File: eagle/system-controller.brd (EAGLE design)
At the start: 99 x 100 mm, 227 parts, among them J1 1, Q1 MOSFET-P-N-PAIR, Q10 MOSFET-P-N-PAIR, Q11 DNP/NTR4101P, Q2 MOSFET-P-N-PAIR, Q3 DON3035L, Q4 MOSFET-P-N-PAIR, Q5 MOSFET-P-N-PAIR, Q6 MOSFET-P-N-PAIR, Q7 MOSFET-P-N-PAIR, Q8 MOSFET-P-N-PAIR, Q9 DNP/NTR4101P, U1 TPS25944LRVCRWQFN-20-3X4, U10 TPS25944LRVCRWQFN-20-3X4, U11 ACPL-M61L, U12 ACPL-M61L, U13 TPS25944LRVCRWQFN-20-3X4, U14 ACPL-M61L, U15 ACPL-M61L, U2 LP5907MFX-3.0, U3 TPS25944LRVCRWQFN-20-3X4, U4 TPS25944LRVCRWQFN-20-3X4, U5 TPS25944LRVCRWQFN-20-3X4, U6 TPS25944LRVCRWQFN-20-3X4, U7 ATMEGA128L-8A(U/N), U8 TS4100, U9 TPS25944LRVCRWQFN-20-3X4, X1 8 MHz CRYSTAL-ABRACON-ABM3-SMD

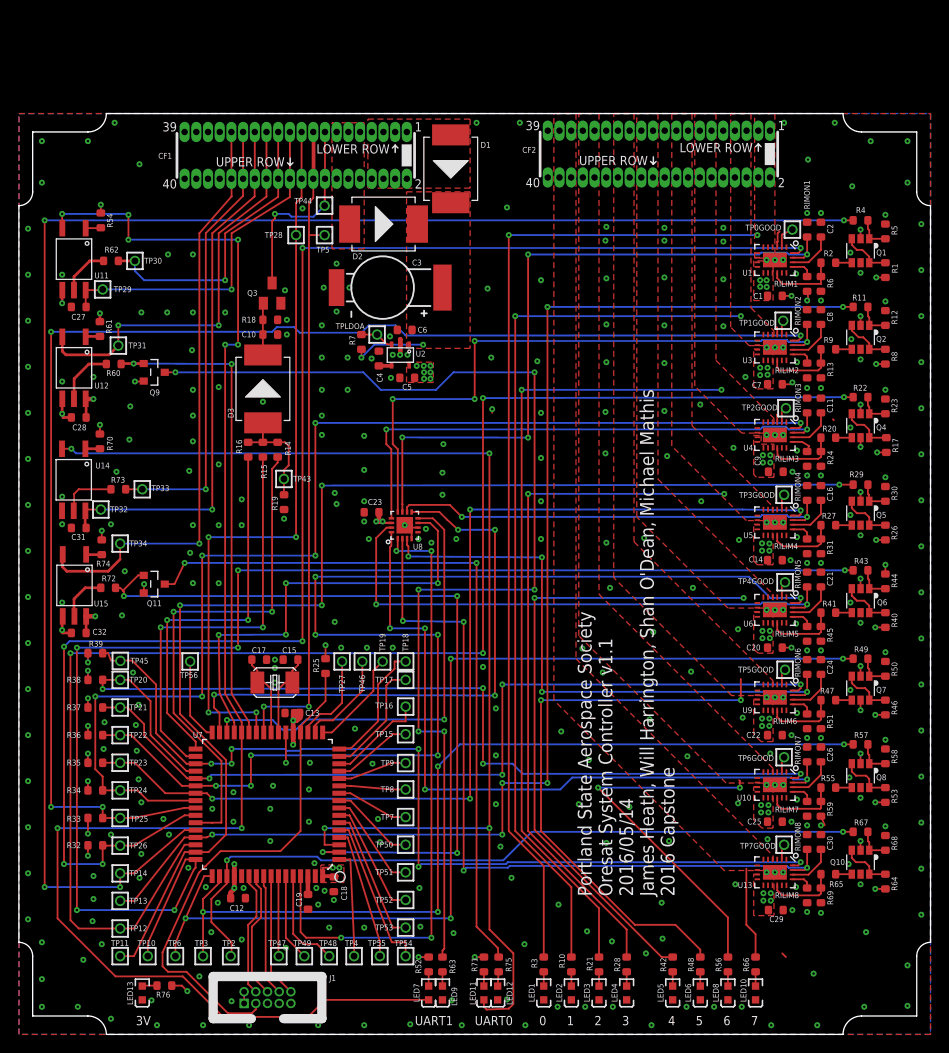
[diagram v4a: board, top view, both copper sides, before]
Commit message: added missing datasheets
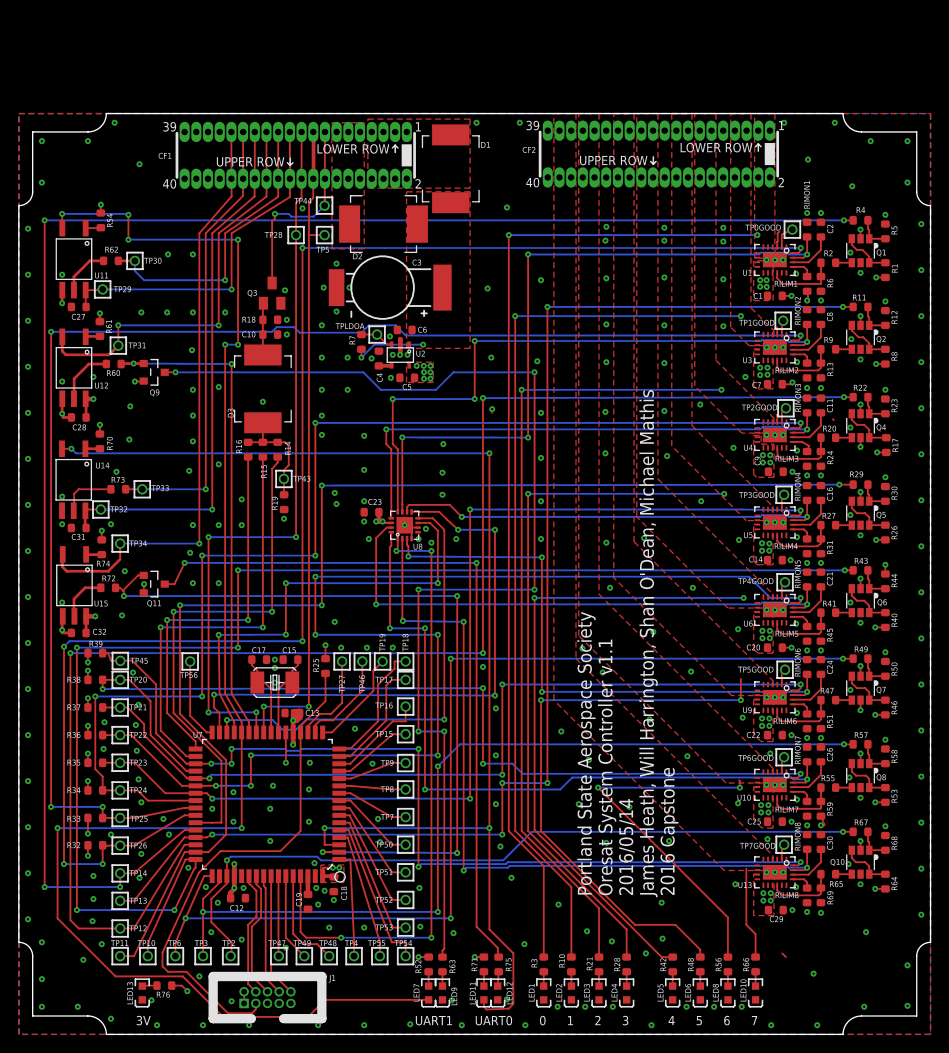
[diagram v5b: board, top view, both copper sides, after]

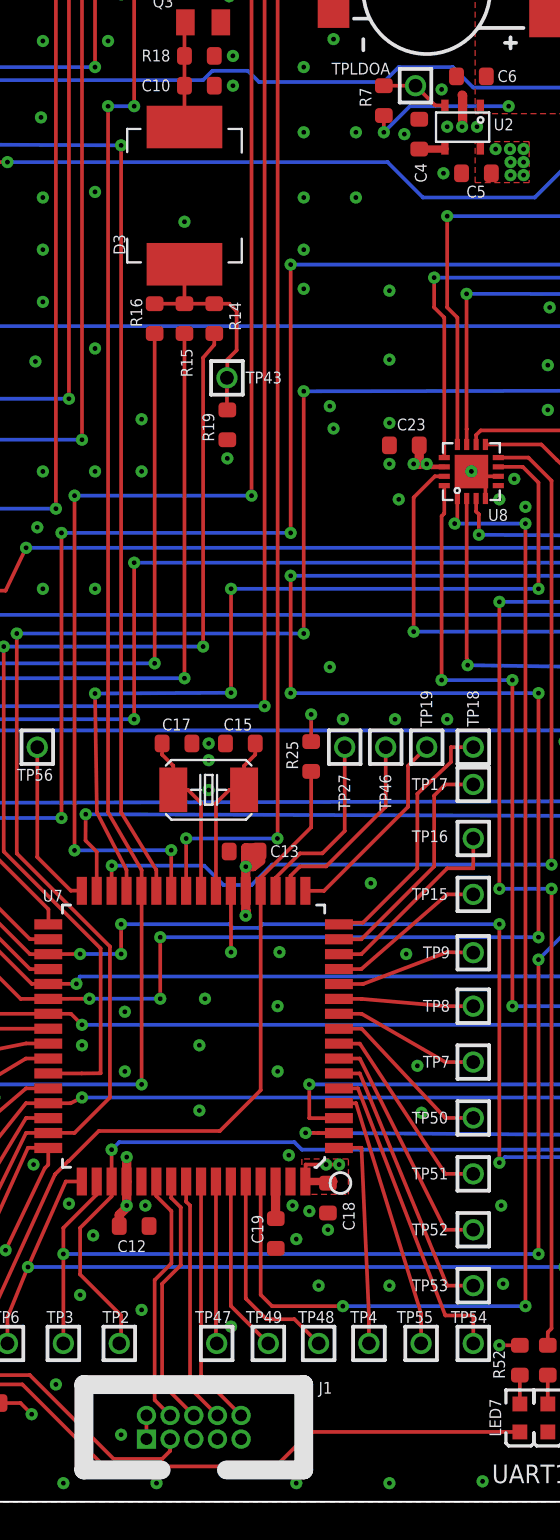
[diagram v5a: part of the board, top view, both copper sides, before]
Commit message: Fixed some of the remaining issues such as JTAG layout and schematic, 0 ohm resistors, etc. Check the issue section on the git for more info
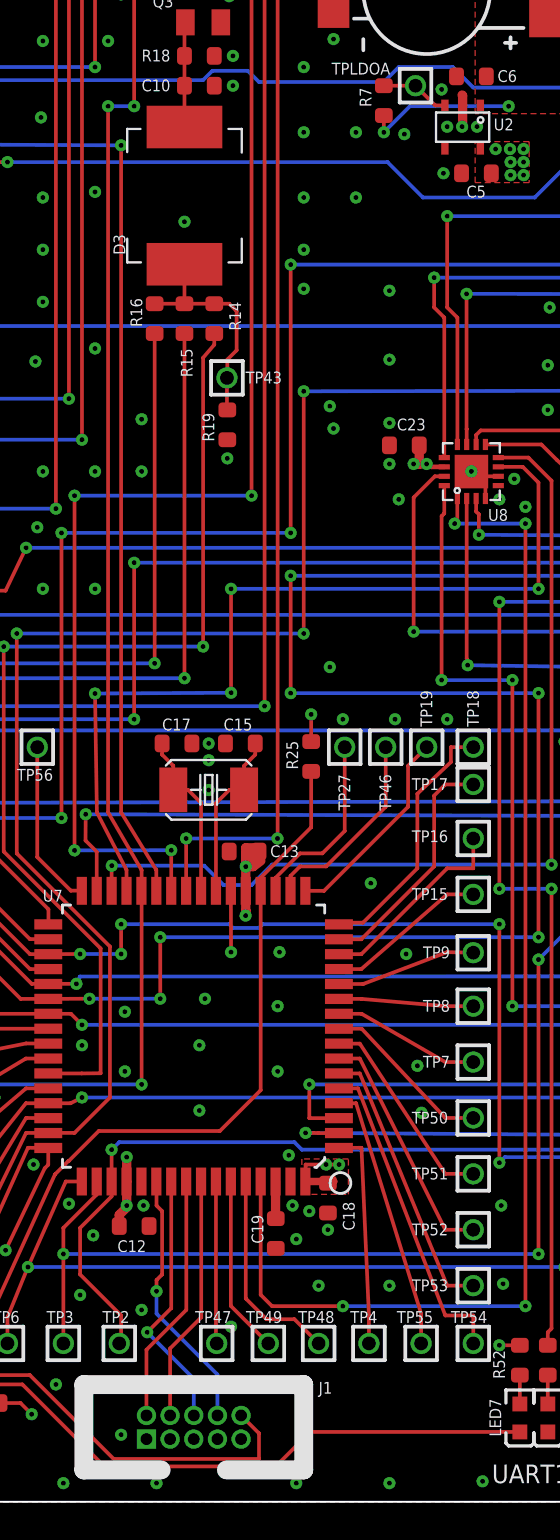
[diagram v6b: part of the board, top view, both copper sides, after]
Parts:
- removed C4: 10nF, rcl_custom:.0603-B-NOSILK
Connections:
- removed net N$23: C4.1, U2.4
- net 3V: no longer J1.2
- net GND: now also J1.3, J1.5; no longer C4.2, J1.7
- net N$11: now also J1.4; no longer J1.10
- net N$13: now also U7.54; no longer U7.56
- net N$14: now also J1.2, U7.56; no longer J1.4, U7.54
- net N$15: now also J1.10; no longer J1.3
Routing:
- net N$15: track 55.3 -> 61.9 mm
- net N$23: track 1.38 -> 0.00 mm
- net 3V: track 46.7 -> 45.5 mm
- net N$13: track 13.3 -> 14.2 mm, vias 0 -> 1
- net N$12: track 13.9 -> 14.1 mm, vias 0 -> 1
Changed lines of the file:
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@@
 <?xml version="1.0" encoding="utf-8"?>
 <!DOCTYPE eagle SYSTEM "eagle.dtd">
-<eagle version="7.5.0">
+<eagle version="7.6.0">
 <drawing>
 <settings>
@@
 <attribute name="NAME" x="42.17" y="71.3" size="0.3" layer="33" ratio="15" rot="R180" align="center"/>
 </element>
-<element name="C4" library="rcl_custom" package=".0603-B-NOSILK" value="10nF" x="39.1" y="73.4" smashed="yes" rot="R90">
-<attribute name="DIST" value="digikey" x="39.1" y="73.4" size="1.778" layer="27" rot="R90" display="off"/>
-<attribute name="DPN" value="399-1092-1-ND" x="39.1" y="73.4" size="1.778" layer="27" rot="R90" display="off"/>
-<attribute name="MFN" value="Kemet" x="39.1" y="73.4" size="1.778" layer="27" rot="R90" display="off"/>
-<attribute name="MPN" value="C0603C103J5RACTU" x="39.1" y="73.4" size="1.778" layer="27" rot="R90" display="off"/>
-<attribute name="NAME" x="39.5" y="70.8" size="0.635" layer="25" font="vector" ratio="20" rot="R90"/>
-<attribute name="VALUE" x="39.8" y="75.2" size="0.635" layer="27" font="vector" ratio="15" rot="R90"/>
-<attribute name="NAME" x="39.1" y="73.4" size="0.3" layer="33" ratio="15" rot="R90" align="center"/>
-</element>
 <element name="C15" library="rcl_custom" package=".0603-B-NOSILK" value="9pF" x="29.5" y="40.7" smashed="yes">
 <attribute name="DIST" value="digikey" x="29.5" y="40.7" size="1.778" layer="27" display="off"/>
@@
 <via x="43.9" y="74.9" extent="1-16" drill="0.254"/>
 </signal>
-<signal name="N$11">
-<contactref element="U7" pad="57"/>
-<contactref element="J1" pad="10"/>
-<wire x1="27.39" y1="17.19" x2="27.39" y2="6.785" width="0.2" layer="1"/>
-<wire x1="27.39" y1="6.785" x2="29.54" y2="4.635" width="0.2" layer="1"/>
-</signal>
-<signal name="N$12">
-<contactref element="U7" pad="55"/>
-<contactref element="J1" pad="6"/>
-<wire x1="25.3" y1="6.335" x2="27" y2="4.635" width="0.2" layer="1"/>
-<wire x1="25.79" y1="17.19" x2="25.79" y2="16.31" width="0.2" layer="1"/>
-<wire x1="25.79" y1="16.31" x2="26.3" y2="15.8" width="0.2" layer="1"/>
-<wire x1="26.3" y1="15.8" x2="26.3" y2="12.7" width="0.2" layer="1"/>
-<wire x1="26.3" y1="12.7" x2="25.3" y2="11.7" width="0.2" layer="1"/>
-<wire x1="25.3" y1="11.7" x2="25.3" y2="6.335" width="0.2" layer="1"/>
-</signal>
-<signal name="N$13">
-<contactref element="U7" pad="56"/>
-<contactref element="J1" pad="8"/>
-<wire x1="26.59" y1="17.19" x2="26.59" y2="16.11" width="0.2" layer="1"/>
-<wire x1="26.59" y1="16.11" x2="26.8" y2="15.9" width="0.2" layer="1"/>
-<wire x1="26.8" y1="15.9" x2="26.8" y2="6.105" width="0.2" layer="1"/>
-<wire x1="26.8" y1="6.105" x2="28.27" y2="4.635" width="0.2" layer="1"/>
-</signal>
-<signal name="N$14">
-<contactref element="U7" pad="54"/>
-<contactref element="J1" pad="4"/>
-<wire x1="24.9" y1="5.465" x2="25.73" y2="4.635" width="0.2" layer="1"/>
-<wire x1="24.99" y1="17.19" x2="24.99" y2="16.41" width="0.2" layer="1"/>
-<wire x1="24.99" y1="16.41" x2="25.8" y2="15.6" width="0.2" layer="1"/>
-<wire x1="25.8" y1="15.6" x2="25.8" y2="12.8" width="0.2" layer="1"/>
-<wire x1="25.8" y1="12.8" x2="24.9" y2="11.9" width="0.2" layer="1"/>
-<wire x1="24.9" y1="11.9" x2="24.9" y2="5.465" width="0.2" layer="1"/>
-</signal>
 <signal name="N$15">
 <contactref element="U7" pad="20"/>
 <contactref element="R25" pad="2"/>
-<contactref element="J1" pad="3"/>
 <wire x1="19.55" y1="17.57" x2="16.1" y2="10" width="0.2" layer="1"/>
 <wire x1="16.1" y1="10" x2="15.6" y2="8.9" width="0.2" layer="1"/>
@@
 <wire x1="16.2" y1="6.8" x2="18.2" y2="6.8" width="0.2" layer="1"/>
 <wire x1="18.2" y1="6.8" x2="22.7" y2="2.3" width="0.2" layer="1"/>
-<wire x1="22.7" y1="2.3" x2="25.3" y2="2.3" width="0.2" layer="1"/>
-<wire x1="25.3" y1="2.3" x2="25.73" y2="2.73" width="0.2" layer="1"/>
-<wire x1="25.7" y1="3.335" x2="25.73" y2="3.365" width="0.2" layer="1"/>
-<wire x1="25.73" y1="3.365" x2="25.73" y2="2.73" width="0.2" layer="1"/>
+<contactref element="J1" pad="10"/>
+<wire x1="22.7" y1="2.3" x2="30.5" y2="2.3" width="0.2" layer="1"/>
+<wire x1="30.5" y1="2.3" x2="30.5" y2="3.675" width="0.2" layer="1"/>
+<wire x1="30.5" y1="3.675" x2="29.54" y2="4.635" width="0.2" layer="1"/>
 </signal>
 <signal name="PCB3_EN">
@@
 <wire x1="6.1" y1="68.91" x2="5.985" y2="69.025" width="0.2" layer="1"/>
 </signal>
-<signal name="N$23">
-<contactref element="C4" pad="1"/>
-<contactref element="U2" pad="4"/>
-<wire x1="39.1" y1="72.6" x2="40.466" y2="72.6" width="0.4" layer="1"/>
-<wire x1="40.466" y1="72.6" x2="40.478" y2="72.612" width="0.4" layer="1"/>
-</signal>
 <signal name="N$1">
 <contactref element="X1" pad="P$2"/>
@@
 <contactref element="R36" pad="1"/>
 <contactref element="R32" pad="1"/>
-<contactref element="J1" pad="2"/>
 <contactref element="U7" pad="64"/>
 <contactref element="U7" pad="21"/>
 <contactref element="U7" pad="52"/>
-<wire x1="24.46" y1="3.365" x2="24.46" y2="4.635" width="0.2" layer="1"/>
 <polygon width="0.2" layer="15" isolate="0.2" thermals="no">
 <vertex x="6" y="90.5"/>
@@
 <signal name="GND">
 <contactref element="C5" pad="2"/>
-<contactref element="C4" pad="2"/>
 <contactref element="C6" pad="1"/>
 <contactref element="C3" pad="-"/>
@@
 <contactref element="C17" pad="1"/>
 <contactref element="J1" pad="9"/>
-<contactref element="J1" pad="7"/>
 <contactref element="C27" pad="1"/>
 <contactref element="C31" pad="1"/>
@@
 <via x="34.2" y="14.6" extent="1-16" drill="0.254"/>
 <via x="33.2" y="15.6" extent="1-16" drill="0.254"/>
-<via x="24.4" y="15.9" extent="1-16" drill="0.254"/>
+<via x="24.3" y="15.9" extent="1-16" drill="0.254"/>
 <via x="27.8" y="38.2" extent="1-16" drill="0.254"/>
 <via x="27.8" y="40.7" extent="1-16" drill="0.254"/>
@@
 <via x="26.5" y="68.7" extent="1-16" drill="0.254"/>
 <contactref element="LED13" pad="K"/>
+<contactref element="J1" pad="5"/>
+<contactref element="J1" pad="3"/>
 </signal>
 <signal name="N$207">
@@
 <wire x1="13.45" y1="5.3" x2="13.4" y2="5.25" width="0.2" layer="1"/>
 </signal>
+<signal name="N$11">
+<contactref element="J1" pad="4"/>
+<contactref element="U7" pad="57"/>
+<wire x1="25.73" y1="4.635" x2="25.73" y2="8.23" width="0.2" layer="1"/>
+<wire x1="25.73" y1="8.23" x2="27.4" y2="9.9" width="0.2" layer="1"/>
+<wire x1="27.4" y1="9.9" x2="27.4" y2="17.18" width="0.2" layer="1"/>
+<wire x1="27.4" y1="17.18" x2="27.39" y2="17.19" width="0.2" layer="1"/>
+</signal>
+<signal name="N$12">
+<contactref element="J1" pad="6"/>
+<contactref element="U7" pad="55"/>
+<wire x1="27" y1="4.635" x2="27" y2="6.6" width="0.2" layer="16"/>
+<wire x1="27" y1="6.6" x2="24.5" y2="9.1" width="0.2" layer="16"/>
+<via x="24.5" y="9.1" extent="1-16" drill="0.254"/>
+<wire x1="24.5" y1="9.1" x2="25.79" y2="10.39" width="0.2" layer="1"/>
+<wire x1="25.79" y1="10.39" x2="25.79" y2="17.19" width="0.2" layer="1"/>
+</signal>
+<signal name="N$13">
+<contactref element="J1" pad="8"/>
+<contactref element="U7" pad="54"/>
+<wire x1="28.27" y1="4.635" x2="28.27" y2="6.83" width="0.2" layer="16"/>
+<wire x1="28.27" y1="6.83" x2="25" y2="10.1" width="0.2" layer="16"/>
+<wire x1="25" y1="10.1" x2="25" y2="11.3" width="0.2" layer="16"/>
+<via x="25" y="11.3" extent="1-16" drill="0.254"/>
+<wire x1="25" y1="11.3" x2="25" y2="11.9" width="0.2" layer="1"/>
+<wire x1="25" y1="11.9" x2="25.3" y2="12.2" width="0.2" layer="1"/>
+<wire x1="25.3" y1="12.2" x2="25.3" y2="15.6" width="0.2" layer="1"/>
+<wire x1="25.3" y1="15.6" x2="25" y2="15.9" width="0.2" layer="1"/>
+<wire x1="25" y1="15.9" x2="25" y2="17.18" width="0.2" layer="1"/>
+<wire x1="25" y1="17.18" x2="24.99" y2="17.19" width="0.2" layer="1"/>
+</signal>
+<signal name="N$14">
+<contactref element="J1" pad="2"/>
+<contactref element="U7" pad="56"/>
+<wire x1="24.46" y1="4.635" x2="24.46" y2="8.16" width="0.2" layer="1"/>
+<wire x1="24.46" y1="8.16" x2="26.6" y2="10.3" width="0.2" layer="1"/>
+<wire x1="26.6" y1="10.3" x2="26.6" y2="17.18" width="0.2" layer="1"/>
+<wire x1="26.6" y1="17.18" x2="26.59" y2="17.19" width="0.2" layer="1"/>
+</signal>
 </signals>

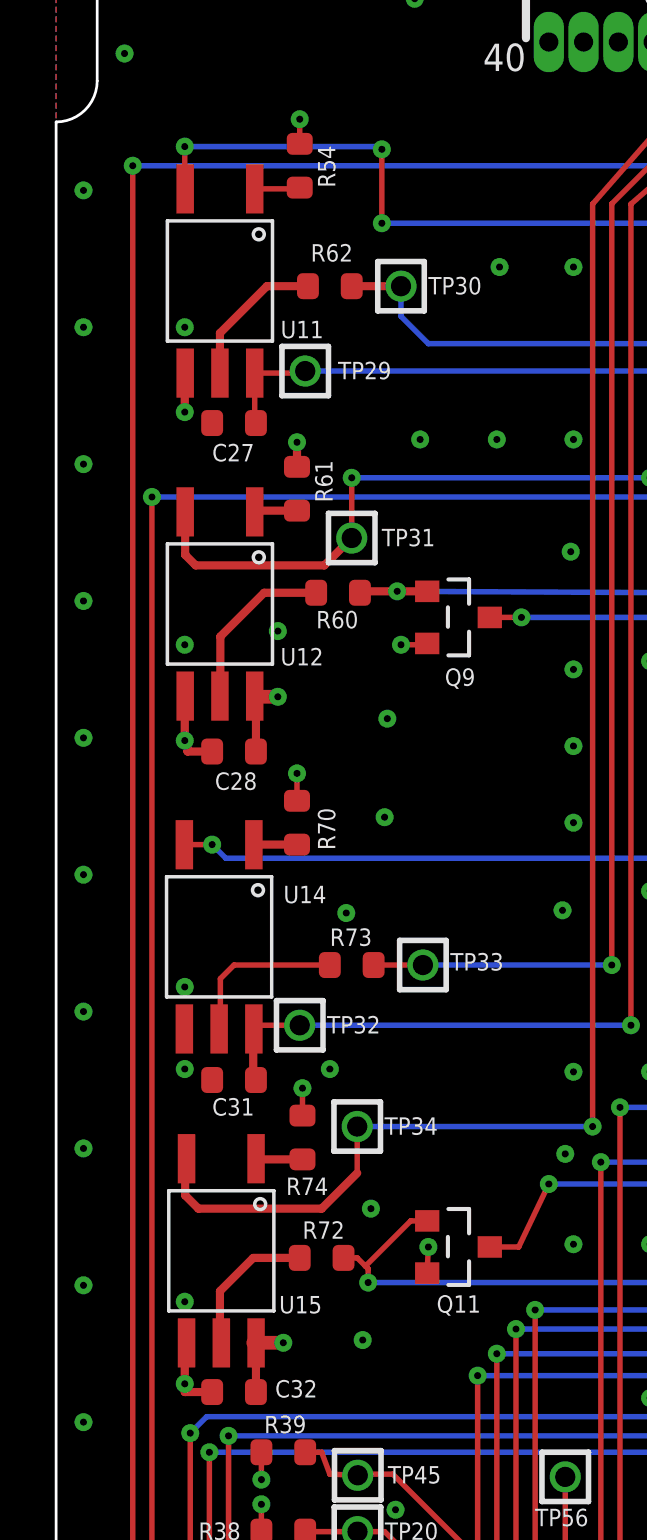
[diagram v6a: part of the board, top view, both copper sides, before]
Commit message: fixed reference designator and origin on optoisolator
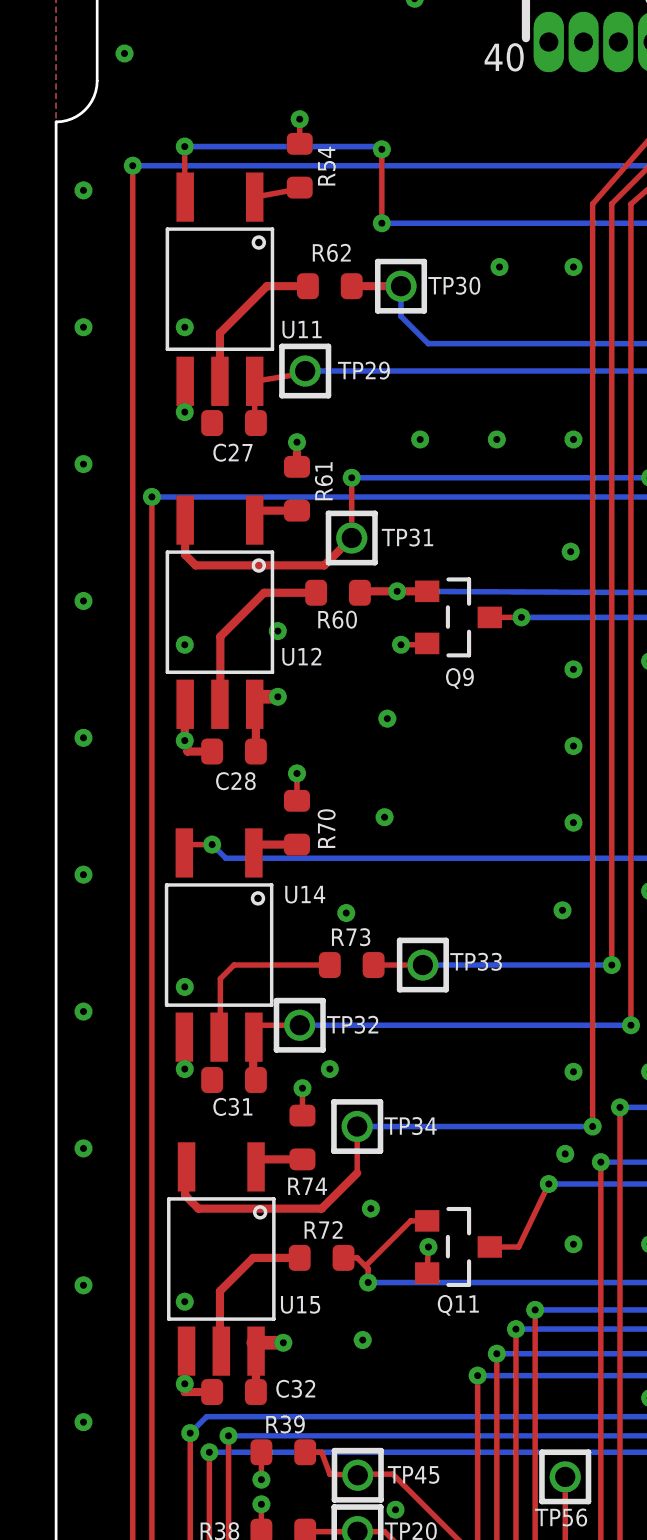
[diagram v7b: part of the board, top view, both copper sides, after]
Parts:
- U11, U12, U14, U15: device system-controller:ACPL-M61L -> v2_sync_box:ACPL-M61L
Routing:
- net GND: track 32.5 -> 33.3 mm
- net N$16: track 6.09 -> 6.65 mm
- net UART_LGR_VCC: track 58.9 -> 59.5 mm
